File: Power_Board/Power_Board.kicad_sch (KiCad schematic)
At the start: 4 parts, among them J1 Conn_01x10, U1 NRF52840-DONGLE

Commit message: few things added
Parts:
- removed J1: Conn_01x10, symbol Connector_Generic:Conn_01x10
- removed J2: (no value), symbol Connector_Generic:Conn_01x10
- removed J3: (no value), symbol Connector:Conn_01x10_Female
- added J1: (no value), symbol Connector:Screw_Terminal_01x02
- added J1_left1: Conn_01x12_Female, symbol Connector:Conn_01x12_Female
- added J1_right1: (no value), symbol Connector:Conn_01x12_Female
- U1: footprint (none) -> MODULE_NRF52840-DONGLE
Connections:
- new net +BATT: J1.2 (Pin_2)
- new net 0.02: J1_right1.8 (Pin_8)
- new net 0.09: J1_left1.10 (Pin_10)
- new net 0.10: J1_left1.11 (Pin_11)
- new net 0.13: J1_left1.3 (Pin_3)
- new net 0.15: J1_left1.4 (Pin_4)
- new net 0.17: J1_left1.5 (Pin_5)
- new net 0.20: J1_left1.6 (Pin_6)
- new net 0.22: J1_left1.7 (Pin_7)
- new net 0.24: J1_left1.8 (Pin_8)
- new net 0.29: J1_right1.7 (Pin_7)
- new net 0.31: J1_right1.6 (Pin_6)
- new net 1.00: J1_left1.9 (Pin_9)
- new net 1.10: J1_right1.11 (Pin_11)
- new net 1.13: J1_right1.10 (Pin_10)
- new net 1.15: J1_right1.9 (Pin_9)
- new net GND: J1.1 (Pin_1), J1_left1.12 (Pin_12), J1_right1.12 (Pin_12), J1_right1.5 (Pin_5)
- new net VBUS: J1_right1.3 (Pin_3)
- new net VDDOUT: J1_right1.4 (Pin_4)
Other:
- note added: "PWR FLAGS"
- note added: "Supercapacitor Storage"
- note added: "To supercap"
- note added: "nRF52840 Dongle"
- company: (none) -> KTH
- title: (none) -> IL2232 - Power Management Board
- moved on the sheet: U1

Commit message: LED added for git test
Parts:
- added D1, D2: LED, symbol Device:LED
- added R1, R2: R, symbol Device:R
- J1: value (none) -> Screw_Terminal_01x02; footprint (none) -> TerminalBlock_RND:TerminalBlock_RND_205-00001_1x02_P5.00mm_Horizontal
- J1_left1: footprint (none) -> Connector_PinSocket_2.54mm:PinSocket_1x12_P2.54mm_Vertical
- J1_right1: value (none) -> Conn_01x12_Female; footprint (none) -> Connector_PinSocket_2.54mm:PinSocket_1x12_P2.54mm_Vertical
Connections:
- net +3V3: now also R1.2, R2.2
- net at U1.0.22: now also D1.1 (K)
- net at U1.0.29: now also D2.1 (K)
- new net: D2.2 (A), R2.1
- new net: D1.2 (A), R1.1
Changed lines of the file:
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@@
     (company "KTH")
   )
+  (wire (pts (xy 180.34 118.11) (xy 179.07 118.11))
+    (stroke (width 0) (type default) (color 0 0 0 0))
+  )
   (polyline (pts (xy 284.48 110.49) (xy 284.48 115.57))
     (stroke (width 0) (type default) (color 0 0 0 0))
@@
     (stroke (width 0) (type default) (color 0 0 0 0))
   )
+  (wire (pts (xy 171.45 113.03) (xy 170.18 113.03))
+    (stroke (width 0) (type default) (color 0 0 0 0))
+  )
   (polyline (pts (xy 284.48 115.57) (xy 284.48 148.59))
     (stroke (width 0) (type default) (color 0 0 0 0))
   )
+  (wire (pts (xy 180.34 113.03) (xy 179.07 113.03))
+    (stroke (width 0) (type default) (color 0 0 0 0))
+  )
   (polyline (pts (xy 26.67 19.05) (xy 26.67 71.12))
     (stroke (width 0) (type default) (color 0 0 0 0))
   )
+  (wire (pts (xy 171.45 118.11) (xy 170.18 118.11))
+    (stroke (width 0) (type default) (color 0 0 0 0))
+  )
   (polyline (pts (xy 26.67 19.05) (xy 91.44 19.05))
     (stroke (width 0) (type default) (color 0 0 0 0))
@@
     (stroke (width 0) (type default) (color 0 0 0 0))
   )
+  (wire (pts (xy 162.56 113.03) (xy 161.29 113.03))
+    (stroke (width 0) (type default) (color 0 0 0 0))
+  )
   (polyline (pts (xy 257.81 148.59) (xy 257.81 110.49))
+    (stroke (width 0) (type default) (color 0 0 0 0))
+  )
+  (wire (pts (xy 162.56 118.11) (xy 161.29 118.11))
     (stroke (width 0) (type default) (color 0 0 0 0))
   )
@@
       (effects (font (size 1.27 1.27)) hide)
     )
-    (property "Value" "" (id 1) (at 274.32 143.51 0))
+    (property "Value" "GND" (id 1) (at 274.32 143.51 0))
     (property "Footprint" "" (id 2) (at 274.32 138.43 0)
       (effects (font (size 1.27 1.27)) hide)
@@
       (effects (font (size 1.27 1.27)) hide)
     )
-    (property "Value" "" (id 1) (at 279.4 119.38 0))
+    (property "Value" "+3V3" (id 1) (at 279.4 119.38 0))
     (property "Footprint" "" (id 2) (at 279.4 124.46 0)
       (effects (font (size 1.27 1.27)) hide)
@@
       (effects (font (size 1.27 1.27)) hide)
     )
-    (property "Value" "" (id 1) (at 267.97 129.54 0))
+    (property "Value" "PWR_FLAG" (id 1) (at 267.97 129.54 0))
     (property "Footprint" "" (id 2) (at 267.97 124.46 0)
       (effects (font (size 1.27 1.27)) hide)
@@
       (effects (font (size 1.27 1.27)) (justify left))
     )
-    (property "Value" "" (id 1) (at 85.09 29.21 0)
+    (property "Value" "Conn_01x12_Female" (id 1) (at 85.09 29.21 0)
       (effects (font (size 1.27 1.27)) (justify left))
     )
-    (property "Footprint" "" (id 2) (at 72.39 45.72 0)
+    (property "Footprint" "Connector_PinSocket_2.54mm:PinSocket_1x12_P2.54mm_Vertical" (id 2) (at 72.39 45.72 0)
       (effects (font (size 1.27 1.27)) hide)
     )
@@
     (pin "9")
   )
+  (symbol (lib_id "power:+3V3") (at 180.34 113.03 0) (unit 1)
+    (in_bom yes) (on_board yes) (fields_autoplaced)
+    (property "Reference" "#PWR0106" (id 0) (at 180.34 116.84 0)
+      (effects (font (size 1.27 1.27)) hide)
+    )
+    (property "Value" "+3V3" (id 1) (at 180.34 107.95 0))
+    (property "Footprint" "" (id 2) (at 180.34 113.03 0)
+      (effects (font (size 1.27 1.27)) hide)
+    )
+    (property "Datasheet" "" (id 3) (at 180.34 113.03 0)
+      (effects (font (size 1.27 1.27)) hide)
+    )
+    (pin "1")
+  )
   (symbol (lib_id "power:GND") (at 134.62 52.07 0) (unit 1)
     (in_bom yes) (on_board yes) (fields_autoplaced)
@@
     (in_bom yes) (on_board yes) (fields_autoplaced)
     (property "Reference" "J1" (id 0) (at 128.27 35.56 0))
-    (property "Value" "" (id 1) (at 128.27 38.1 0))
-    (property "Footprint" "" (id 2) (at 128.27 44.45 0)
+    (property "Value" "Screw_Terminal_01x02" (id 1) (at 128.27 38.1 0))
+    (property "Footprint" "TerminalBlock_RND:TerminalBlock_RND_205-00001_1x02_P5.00mm_Horizontal" (id 2) (at 128.27 44.45 0)
       (effects (font (size 1.27 1.27)) hide)
     )
@@
     (pin "2")
   )
+  (symbol (lib_id "Device:R") (at 175.26 118.11 90) (unit 1)
+    (in_bom yes) (on_board yes)
+    (property "Reference" "R2" (id 0) (at 175.26 123.19 90))
+    (property "Value" "R" (id 1) (at 175.26 120.65 90))
+    (property "Footprint" "" (id 2) (at 175.26 119.888 90)
+      (effects (font (size 1.27 1.27)) hide)
+    )
+    (property "Datasheet" "~" (id 3) (at 175.26 118.11 0)
+      (effects (font (size 1.27 1.27)) hide)
+    )
+    (pin "1")
+    (pin "2")
+  )
   (symbol (lib_id "power:+1V8") (at 267.97 124.46 0) (unit 1)
     (in_bom yes) (on_board yes) (fields_autoplaced)
@@
       (effects (font (size 1.27 1.27)) hide)
     )
-    (property "Value" "" (id 1) (at 267.97 119.38 0))
+    (property "Value" "+1V8" (id 1) (at 267.97 119.38 0))
     (property "Footprint" "" (id 2) (at 267.97 124.46 0)
       (effects (font (size 1.27 1.27)) hide)
     )
     (property "Datasheet" "" (id 3) (at 267.97 124.46 0)
+      (effects (font (size 1.27 1.27)) hide)
+    )
+    (pin "1")
+  )
+  (symbol (lib_id "Device:LED") (at 166.37 118.11 0) (unit 1)
+    (in_bom yes) (on_board yes)
+    (property "Reference" "D2" (id 0) (at 166.37 123.19 0))
+    (property "Value" "LED" (id 1) (at 166.37 120.65 0))
+    (property "Footprint" "" (id 2) (at 166.37 118.11 0)
+      (effects (font (size 1.27 1.27)) hide)
+    )
+    (property "Datasheet" "~" (id 3) (at 166.37 118.11 0)
+      (effects (font (size 1.27 1.27)) hide)
+    )
+    (pin "1")
+    (pin "2")
+  )
+  (symbol (lib_id "power:+3V3") (at 180.34 118.11 0) (unit 1)
+    (in_bom yes) (on_board yes)
+    (property "Reference" "#PWR0107" (id 0) (at 180.34 121.92 0)
+      (effects (font (size 1.27 1.27)) hide)
+    )
+    (property "Value" "+3V3" (id 1) (at 180.34 120.65 0))
+    (property "Footprint" "" (id 2) (at 180.34 118.11 0)
+      (effects (font (size 1.27 1.27)) hide)
+    )
+    (property "Datasheet" "" (id 3) (at 180.34 118.11 0)
       (effects (font (size 1.27 1.27)) hide)
     )
@@
       (effects (font (size 1.27 1.27)) (justify left))
     )
-    (property "Footprint" "" (id 2) (at 57.15 45.72 0)
+    (property "Footprint" "Connector_PinSocket_2.54mm:PinSocket_1x12_P2.54mm_Vertical" (id 2) (at 57.15 45.72 0)
       (effects (font (size 1.27 1.27)) hide)
     )
@@
       (effects (font (size 1.27 1.27)) hide)
     )
-    (property "Value" "" (id 1) (at 142.24 29.21 0))
+    (property "Value" "+BATT" (id 1) (at 142.24 29.21 0))
     (property "Footprint" "" (id 2) (at 142.24 34.29 0)
       (effects (font (size 1.27 1.27)) hide)
@@
     )
     (pin "1")
+  )
+  (symbol (lib_id "Device:LED") (at 166.37 113.03 0) (unit 1)
+    (in_bom yes) (on_board yes)
+    (property "Reference" "D1" (id 0) (at 166.37 107.95 0))
+    (property "Value" "LED" (id 1) (at 166.37 110.49 0))
+    (property "Footprint" "" (id 2) (at 166.37 113.03 0)
+      (effects (font (size 1.27 1.27)) hide)
+    )
+    (property "Datasheet" "~" (id 3) (at 166.37 113.03 0)
+      (effects (font (size 1.27 1.27)) hide)
+    )
+    (pin "1")
+    (pin "2")
+  )
+  (symbol (lib_id "Device:R") (at 175.26 113.03 90) (unit 1)
+    (in_bom yes) (on_board yes) (fields_autoplaced)
+    (property "Reference" "R1" (id 0) (at 175.26 106.68 90))
+    (property "Value" "R" (id 1) (at 175.26 109.22 90))
+    (property "Footprint" "" (id 2) (at 175.26 114.808 90)
+      (effects (font (size 1.27 1.27)) hide)
+    )
+    (property "Datasheet" "~" (id 3) (at 175.26 113.03 0)
+      (effects (font (size 1.27 1.27)) hide)
+    )
+    (pin "1")
+    (pin "2")
   )
   (sheet_instances
@@
       (reference "#PWR0105") (unit 1) (value "+BATT") (footprint "")
     )
+    (path "/6ba8b8cf-3873-4ded-9b2d-166f42b2a14d"
+      (reference "#PWR0106") (unit 1) (value "+3V3") (footprint "")
+    )
+    (path "/9dcd14f8-fd45-46a8-867c-7bb2afc3c15d"
+      (reference "#PWR0107") (unit 1) (value "+3V3") (footprint "")
+    )
+    (path "/dcea4094-c268-4a59-895a-8f4c38df7bc2"
+      (reference "D1") (unit 1) (value "LED") (footprint "LED_THT:LED_D5.0mm")
+    )
+    (path "/8c98edd9-b71c-4767-98e4-a7105052d6a0"
+      (reference "D2") (unit 1) (value "LED") (footprint "LED_THT:LED_D5.0mm")
+    )
     (path "/7059482a-1ab5-41af-a31c-5533b284b340"
       (reference "J1") (unit 1) (value "Screw_Terminal_01x02") (footprint "TerminalBlock_RND:TerminalBlock_RND_205-00001_1x02_P5.00mm_Horizontal")
@@
       (reference "J1_right1") (unit 1) (value "Conn_01x12_Female") (footprint "Connector_PinSocket_2.54mm:PinSocket_1x12_P2.54mm_Vertical")
     )
+    (path "/eb733ded-c124-4d74-ae22-95c1c0168b64"
+      (reference "R1") (unit 1) (value "R") (footprint "OptoDevice:R_LDR_5.2x5.2mm_P3.5mm_Horizontal")
+    )
+    (path "/75526153-2e21-4194-81bf-5050ab77a12a"
+      (reference "R2") (unit 1) (value "R") (footprint "OptoDevice:R_LDR_5.2x5.2mm_P3.5mm_Horizontal")
+    )
     (path "/16ae8da5-0a27-45ca-969e-e51f0a1d0ac2"

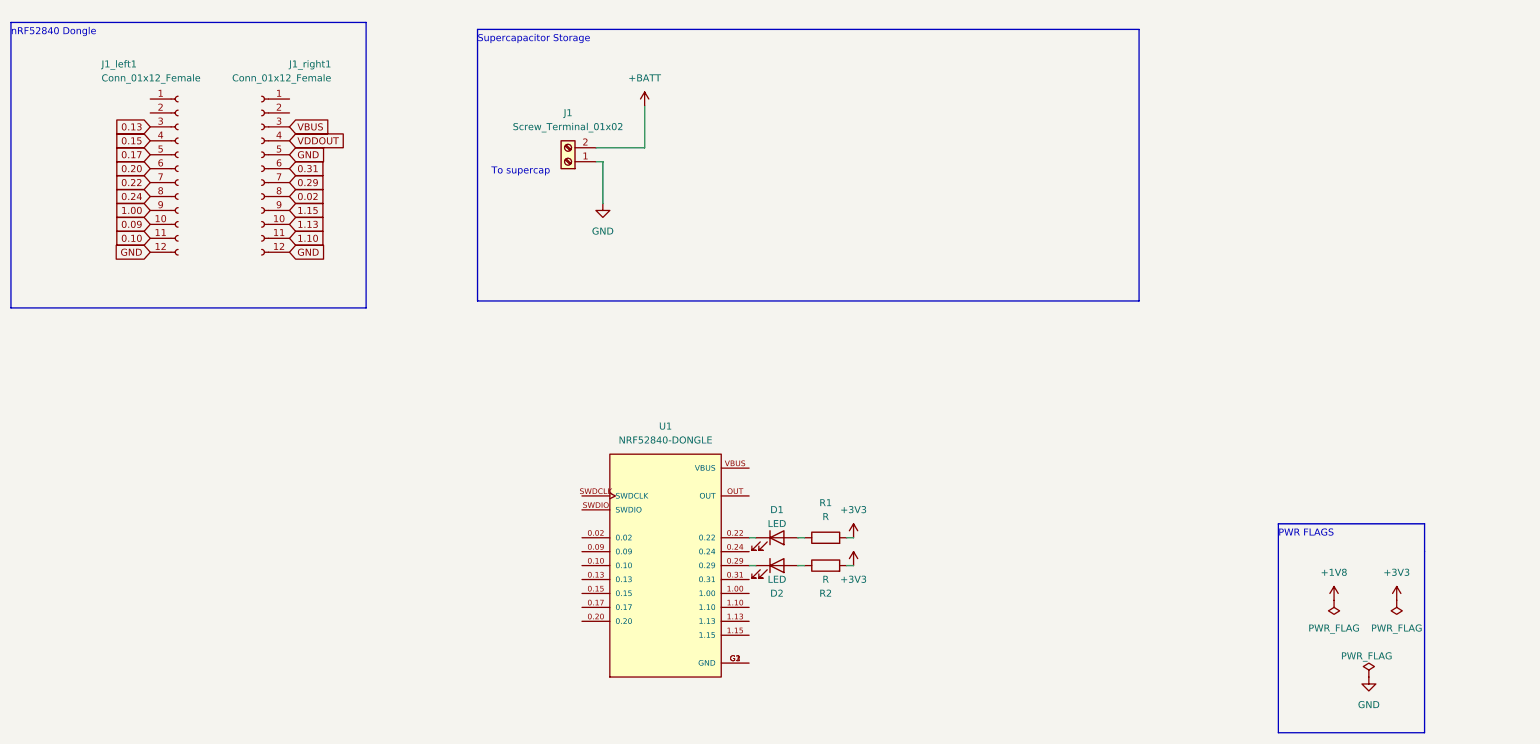
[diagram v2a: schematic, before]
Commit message: sensor adeed
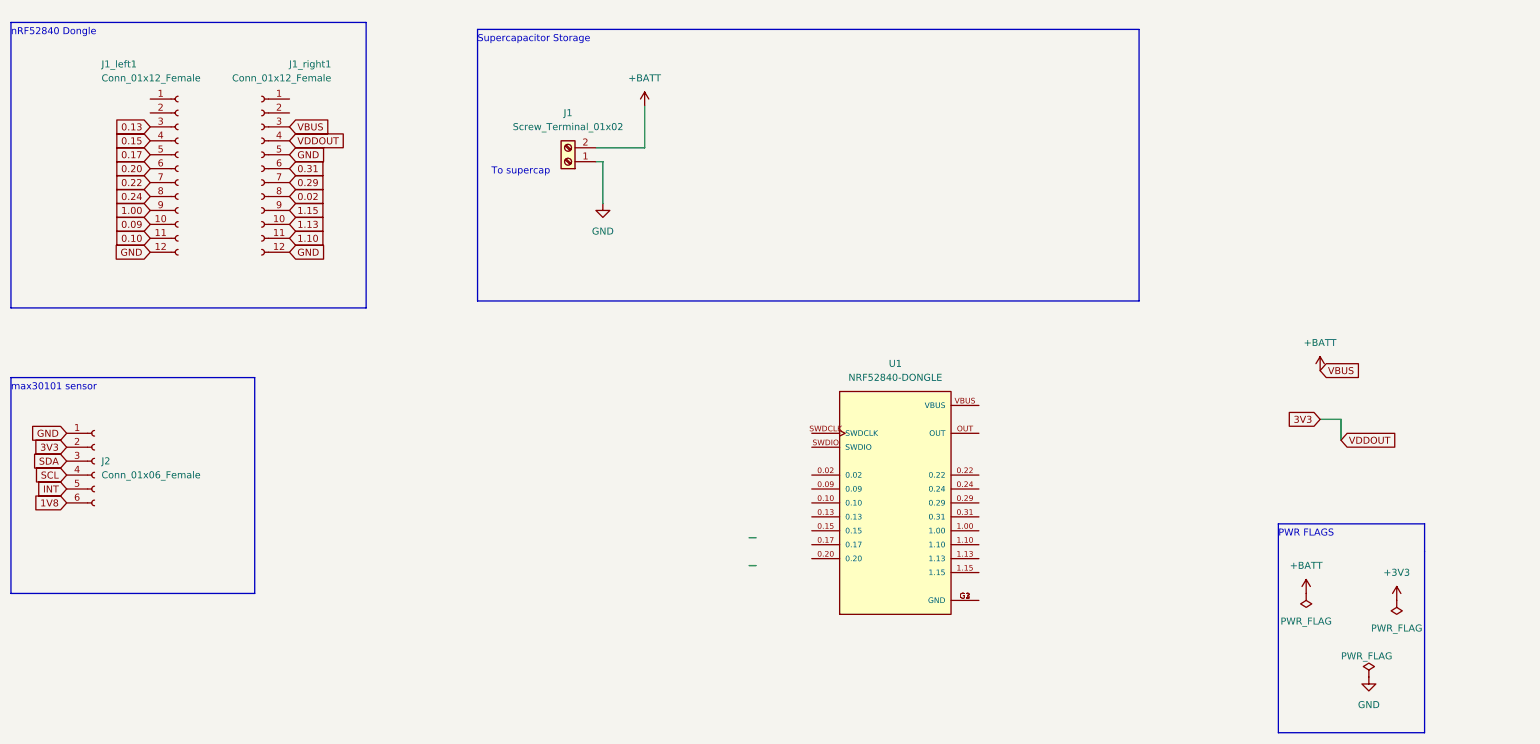
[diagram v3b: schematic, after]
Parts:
- removed D1, D2: LED, symbol Device:LED
- removed R1, R2: R, symbol Device:R
- added J2: Conn_01x06_Female, Connector_PinSocket_2.54mm:PinSocket_1x06_P2.54mm_Vertical, symbol Connector:Conn_01x06_Female
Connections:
- net VBUS is gone; now on net +BATT: J1_right1.3 (Pin_3)
- net GND: now also J2.1 (Pin_1)
- net VDDOUT renamed 3V3
- net 3V3: now also J2.2 (Pin_2)
- new net 1V8: J2.6 (Pin_6)
- new net INT: J2.5 (Pin_5)
- new net SCL: J2.4 (Pin_4)
- new net SDA: J2.3 (Pin_3)
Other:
- note added: "max30101 sensor"
- moved on the sheet: U1

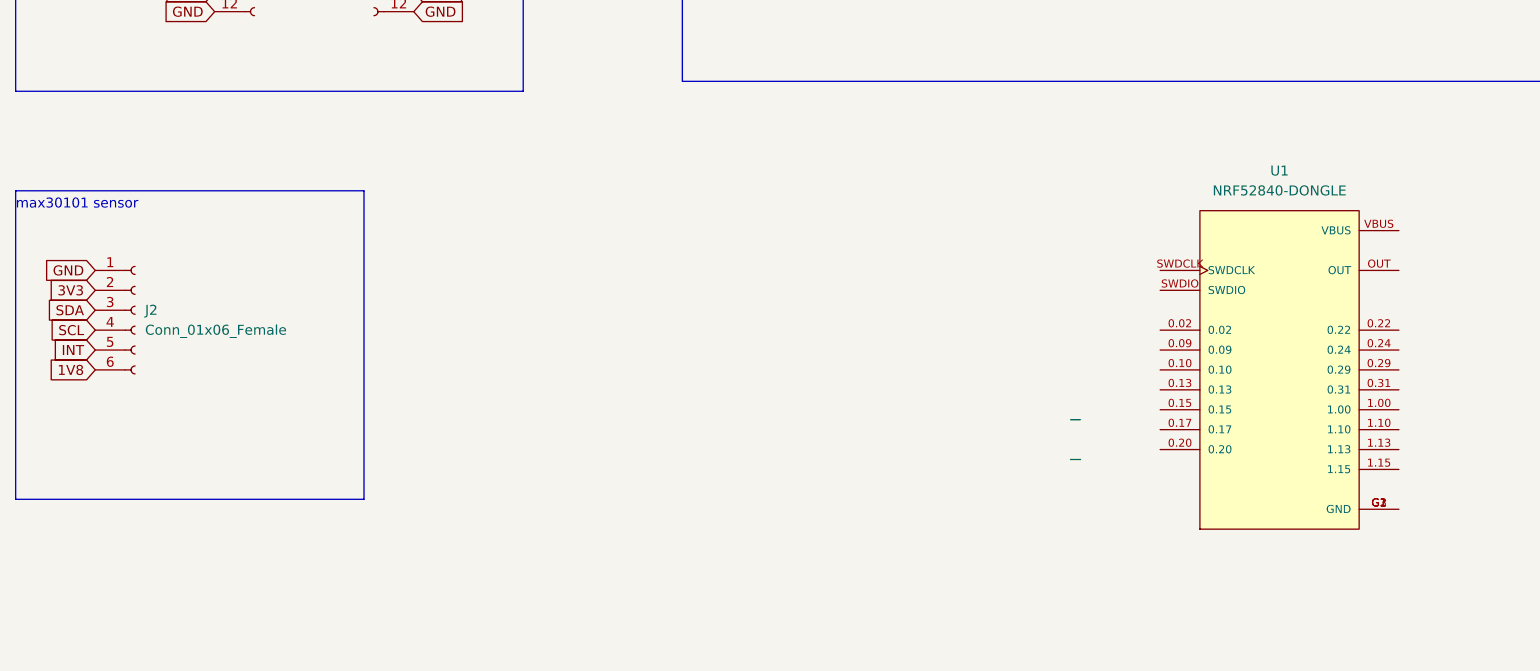
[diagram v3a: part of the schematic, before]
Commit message: rectifier added
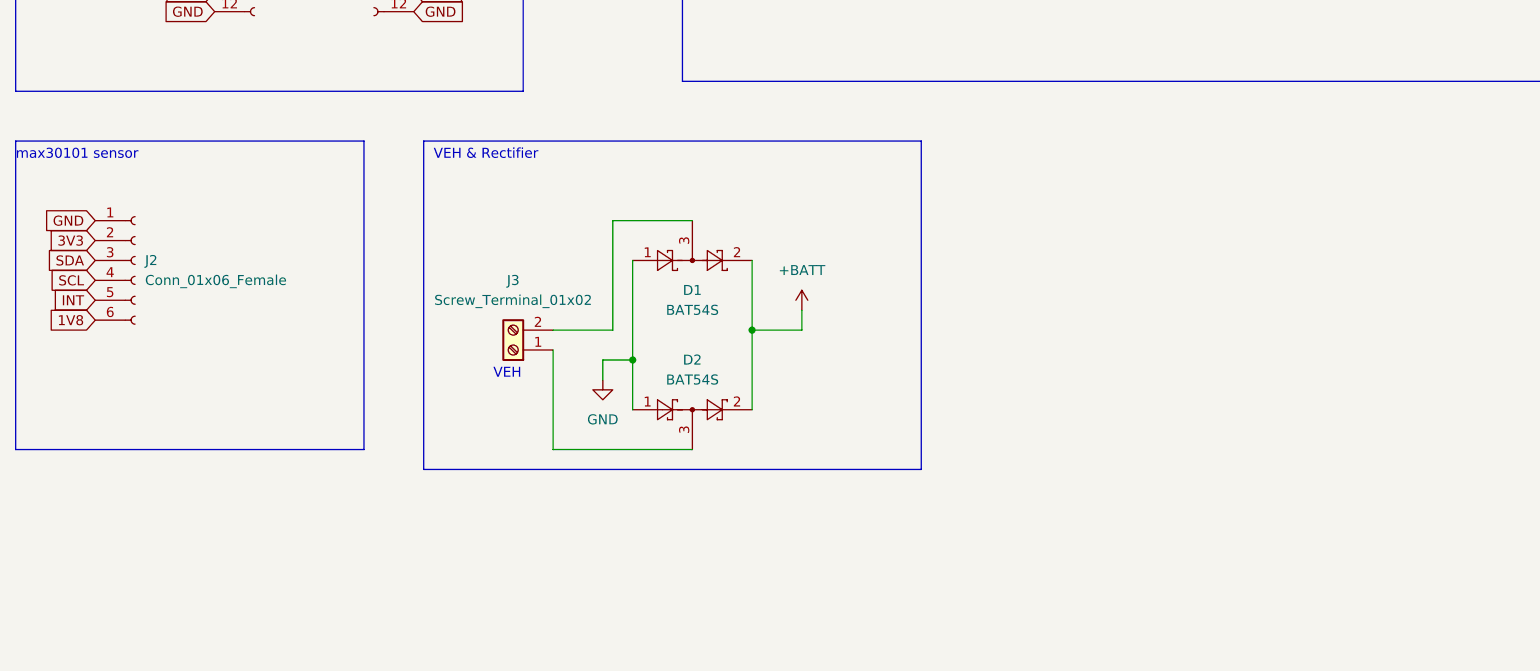
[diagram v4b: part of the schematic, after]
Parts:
- removed U1: NRF52840-DONGLE, MODULE_NRF52840-DONGLE, symbol NRF52840-DONGLE:NRF52840-DONGLE
- added D1, D2: BAT54S, Package_TO_SOT_SMD:SOT-23, symbol Diode:BAT54S
- added J3: Screw_Terminal_01x02, TerminalBlock_RND:TerminalBlock_RND_205-00001_1x02_P5.00mm_Horizontal, symbol Connector:Screw_Terminal_01x02
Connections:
- net +BATT: now also D1.2, D2.2
- net GND: now also D1.1, D2.1
- new net: D2.3, J3.1 (Pin_1)
- new net: D1.3, J3.2 (Pin_2)
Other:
- note added: "VEH"
- note added: "VEH & Rectifier"
- moved on the sheet: J2
